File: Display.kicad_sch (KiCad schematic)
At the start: 34 parts, among them J2 2.54 mm header, J3 Conn_01x14_Pin

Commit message: updated sch template (A4)
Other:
- note removed: "${SHEETNAME}"
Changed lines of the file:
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@@
-		)
-	)
-	(text "${SHEETNAME}"
-		(exclude_from_sim no)
-		(at 283.21 14.605 0)
-		(effects
-			(font
-				(face "DejaVu Sans")
-				(size 3.81 3.81)
-				(bold yes)
-				(color 0 0 0 1)
-			)
-			(justify right top)
 		)
 	)
@@
 				(size 2.032 2.032)
 				(thickness 0.3175)
-				(color 0 0 0 1)
+				(color 0 0 194 1)
 			)
 			(justify left bottom)

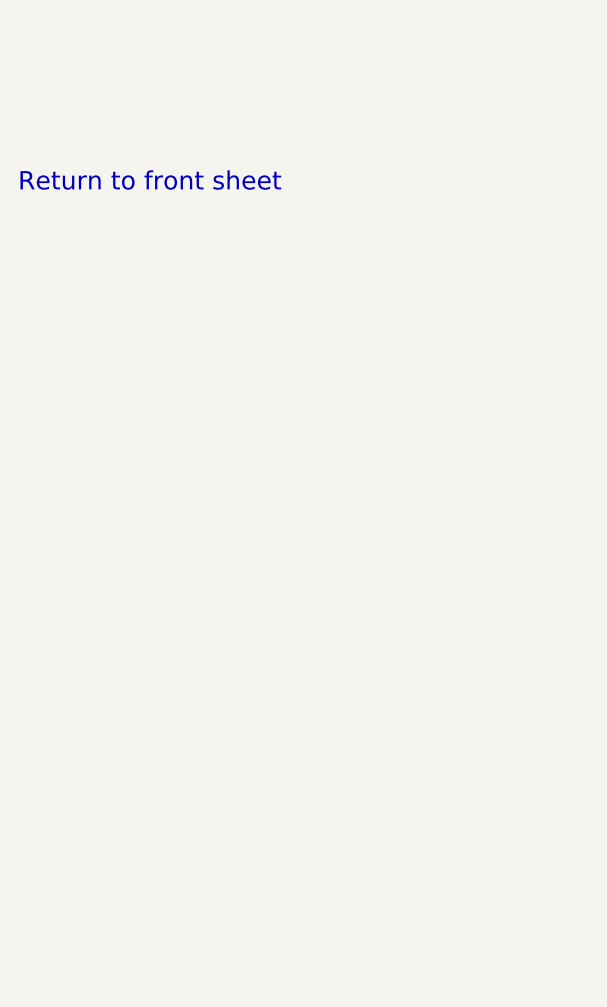
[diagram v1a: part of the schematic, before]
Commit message: new sch size
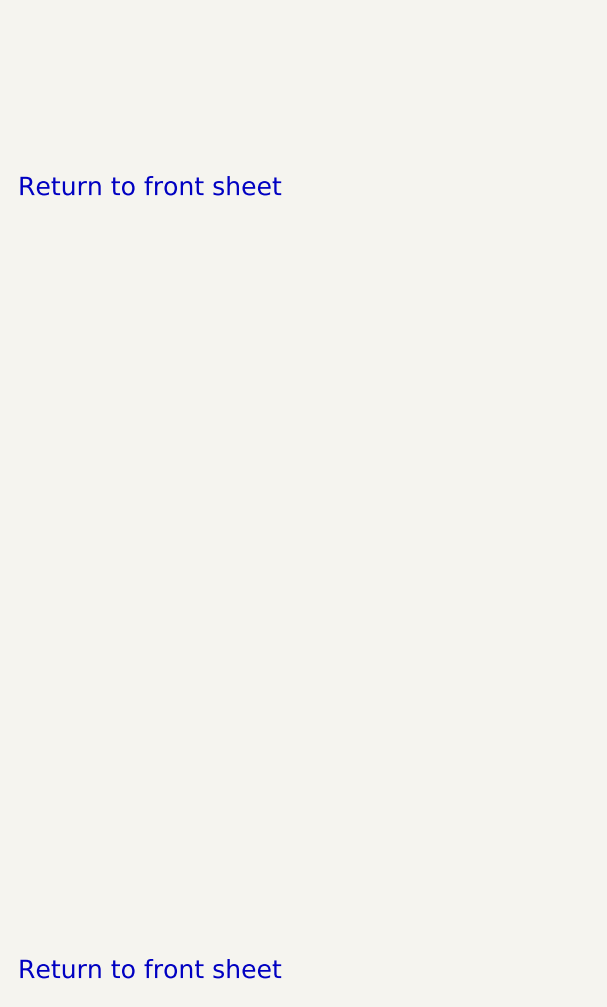
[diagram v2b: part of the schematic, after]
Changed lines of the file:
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@@
 	(generator "eeschema")
 	(generator_version "10.0")
-	(paper "A4")
+	(paper "A3")
 	(rectangle
 		(start 13.97 13.97)
@@
 	(text "Return to front sheet"
 		(exclude_from_sim no)
-		(at 12.7 197.485 0)
+		(at 12.7 285.115 0)
 		(effects
 			(font
+				(face "DejaVu Sans")
+				(size 2.032 2.032)
+				(thickness 0.3175)
+				(color 0 0 194 1)
+			)
+			(justify left bottom)
+			(href "#1")
+		)
+	)
+	(text "Return to front sheet"
+		(exclude_from_sim no)
+		(at 12.7 198.12 0)
+		(effects
+			(font

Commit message: adding more outputs
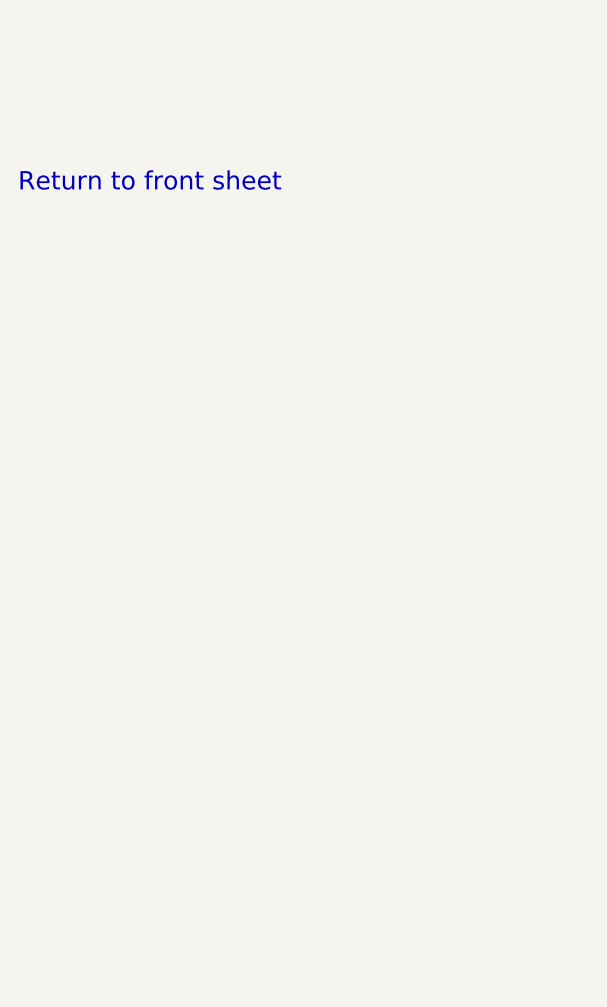
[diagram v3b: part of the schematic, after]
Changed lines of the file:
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@@
 	(generator "eeschema")
 	(generator_version "10.0")
-	(paper "A3")
+	(paper "A4")
 	(rectangle
 		(start 13.97 13.97)
@@
 	(text "Return to front sheet"
 		(exclude_from_sim no)
-		(at 12.7 285.115 0)
+		(at 12.7 197.485 0)
 		(effects
 			(font
-				(face "DejaVu Sans")
-				(size 2.032 2.032)
-				(thickness 0.3175)
-				(color 0 0 194 1)
-			)
-			(justify left bottom)
-			(href "#1")
-		)
-	)
-	(text "Return to front sheet"
-		(exclude_from_sim no)
-		(at 12.7 198.12 0)
-		(effects
-			(font

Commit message: supplier and mpn added
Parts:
- C1: Manufacturer (none) -> Yageo; Manufacturer Part Number (none) -> AC0603KRX7R9BB104
- J2: value 2.54 mm header -> 01x04 socket; Manufacturer (none) -> Generic; Manufacturer Part Number (none) -> Generic
- J3: value Conn_01x14_Pin -> 01x14 socket; Manufacturer (none) -> Generic; Manufacturer Part Number (none) -> Generic
- P1, P10, P11, P2, P3, P4, P5, P6, P7, P78, P79, P8, P80, P83, P84, P85, P86, P87, P9: Manufacturer (none) -> NA; Manufacturer Part Number (none) -> NA
- TFT1: Manufacturer (none) -> TENSTAR ROBOT; Manufacturer Part Number (none) -> ILI9341_320x240
